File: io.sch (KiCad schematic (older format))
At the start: 14 parts, among them J5 USB_C_Receptacle_USB2.0, J6 Conn_ARM_JTAG_SWD_10, J7 UART, J8 Conn_02x14_Top_Bottom

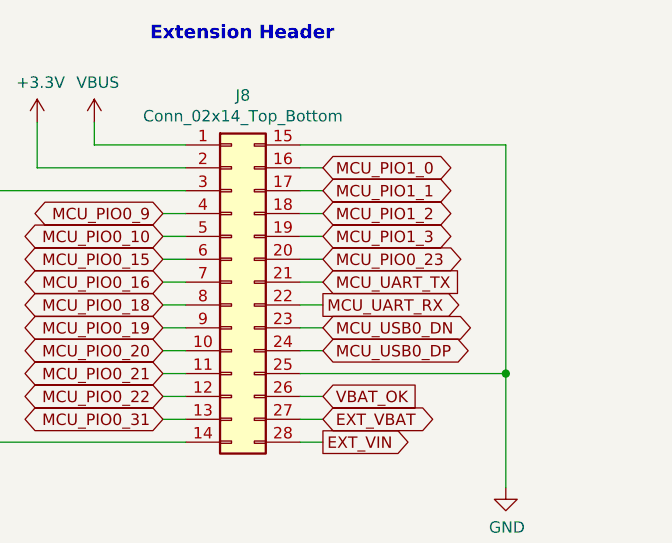
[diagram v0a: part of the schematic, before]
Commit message: Fixed issue #2, #3, #4 and #5
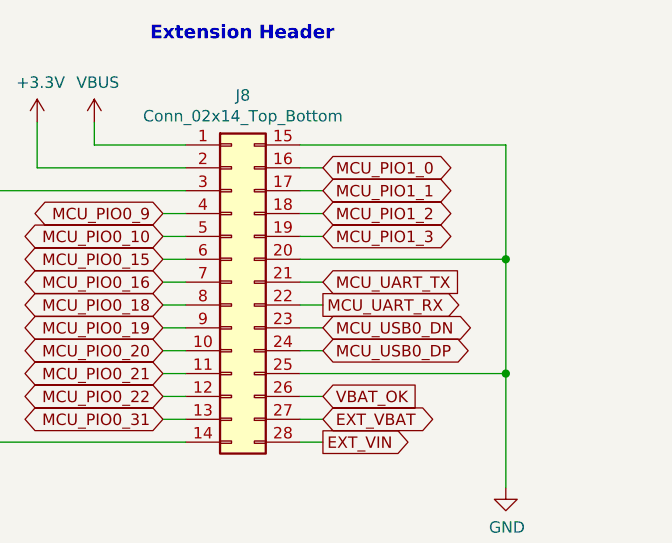
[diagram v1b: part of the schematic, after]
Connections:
- net MCU_PIO0_23 is gone; now on net GND: J8.20 (Pin_20)
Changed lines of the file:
@@
 Sheet 6 6
 Title "Tardigrade"
-Date "2020-09-24"
+Date "2020-11-05"
 Rev "1.0"
 Comp "Lucerne University of Applied Sciences and Arts"
@@
 	3700 1600 4000 1600
 Wire Wire Line
-	9200 1650 9200 2650
-Text GLabel 8400 2150 2    50   BiDi ~ 0
-MCU_PIO0_23
-Wire Wire Line
-	8400 2150 8300 2150
+	9200 1650 9200 2150
 Wire Wire Line
 	3350 1600 3400 1600
@@
 	1    0    0    -1
 $EndComp
+Wire Wire Line
+	8300 2150 9200 2150
+Connection ~ 9200 2150
+Wire Wire Line
+	9200 2150 9200 2650
 $EndSCHEMATC

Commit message: Removed jumpers from ios
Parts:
- removed JP15: Jumper_NC_Small, Jumper:SolderJumper-2_P1.3mm_Bridged_Pad1.0x1.5mm, symbol Device:Jumper_NC_Small
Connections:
- net +3V3: now also J6.1 (VTref)
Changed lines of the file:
@@
 Wire Wire Line
 	3450 5950 3450 5900
-$Comp
-L Device:Jumper_NC_Small JP?
-U 1 1 5FB371B1
-P 3450 4550
-AR Path="/5F6D82DD/5FB371B1" Ref="JP?"  Part="1"
-AR Path="/5F6D9EB2/5FB371B1" Ref="JP15"  Part="1"
-F 0 "JP15" V 3450 4502 50  0000 R CNN
-F 1 "Jumper_NC_Small" V 3405 4503 50  0001 R CNN
-F 2 "Jumper:SolderJumper-2_P1.3mm_Bridged_Pad1.0x1.5mm" H 3450 4550 50  0001 C CNN
-F 3 "~" H 3450 4550 50  0001 C CNN
-	1    3450 4550
-	0    -1   -1   0
-$EndComp
-Wire Wire Line
-	3450 4700 3450 4650
-Wire Wire Line
-	3450 4450 3450 4400
 Text Notes 2200 6600 0    50   Italic 0
 The JTAG functions TRST, TCK, TMS, TDI, and TDO, are selected \non pins PIO0_2 to PIO0_6 by hardware when the part is in \nboundary scan mode. The JTAG functions cannot be used for \ndebug mode
@@
 Extension Header
 $Comp
-L power:PWR_FLAG #FLG07
-U 1 1 5FCBE7BD
-P 3300 4650
-F 0 "#FLG07" H 3300 4725 50  0001 C CNN
-F 1 "PWR_FLAG" H 3300 4823 50  0001 C CNN
-F 2 "" H 3300 4650 50  0001 C CNN
-F 3 "~" H 3300 4650 50  0001 C CNN
-	1    3300 4650
-	1    0    0    -1
-$EndComp
-Wire Wire Line
-	3450 4700 3300 4700
-Wire Wire Line
-	3300 4700 3300 4650
-Connection ~ 3450 4700
-$Comp
 L Mechanical:MountingHole H?
 U 1 1 5FDA315D
@@
 L power:+3.3V #PWR067
 U 1 1 5F833987
-P 3450 4400
-F 0 "#PWR067" H 3450 4250 50  0001 C CNN
-F 1 "+3.3V" H 3465 4573 50  0000 C CNN
-F 2 "" H 3450 4400 50  0001 C CNN
-F 3 "" H 3450 4400 50  0001 C CNN
-	1    3450 4400
+P 3450 4650
+F 0 "#PWR067" H 3450 4500 50  0001 C CNN
+F 1 "+3.3V" H 3465 4823 50  0000 C CNN
+F 2 "" H 3450 4650 50  0001 C CNN
+F 3 "" H 3450 4650 50  0001 C CNN
+	1    3450 4650
 	1    0    0    -1
 $EndComp
@@
 Wire Wire Line
 	9200 2150 9200 2650
+Wire Wire Line
+	3450 4650 3450 4700
 $EndSCHEMATC

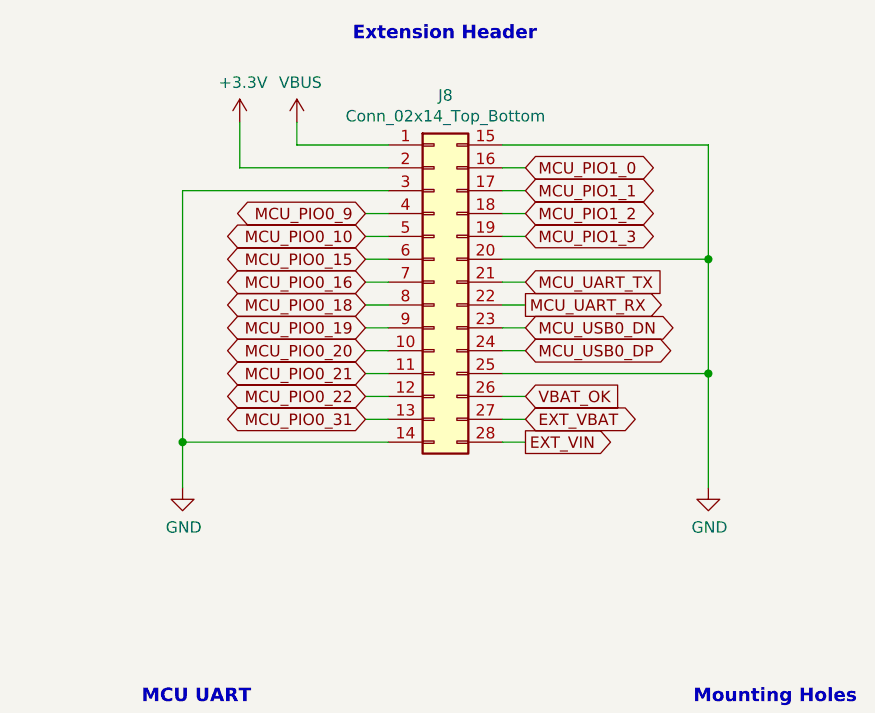
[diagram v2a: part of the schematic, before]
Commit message: Changed extension header symbol
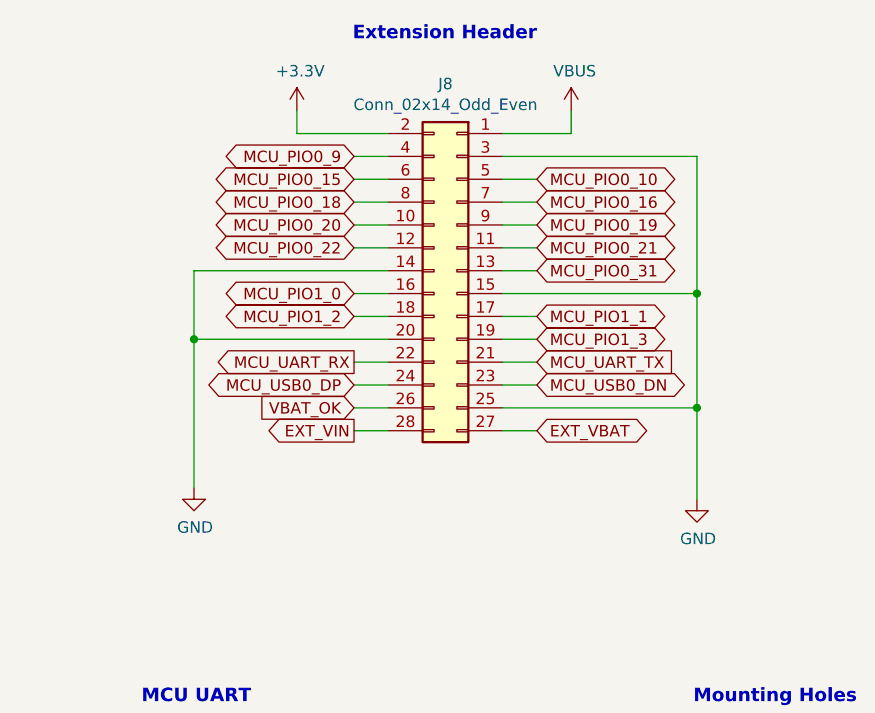
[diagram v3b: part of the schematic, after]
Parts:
- removed J8: Conn_02x14_Top_Bottom, Connector_PinSocket_2.54mm:PinSocket_2x14_P2.54mm_Vertical, symbol Connector_Generic:Conn_02x14_Top_Bottom
- added J8: Conn_02x14_Odd_Even, symbol Connector_Generic:Conn_02x14_Odd_Even
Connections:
- net +3V3: now also J8.2 (Pin_2)
- net EXT_VBAT: now also J8.27 (Pin_27)
- net EXT_VIN: now also J8.28 (Pin_28)
- net GND: now also J8.14 (Pin_14), J8.15 (Pin_15), J8.20 (Pin_20), J8.25 (Pin_25), J8.3 (Pin_3)
- net MCU_PIO0_10: now also J8.5 (Pin_5)
- net MCU_PIO0_15: now also J8.6 (Pin_6)
- net MCU_PIO0_16: now also J8.7 (Pin_7)
- net MCU_PIO0_18: now also J8.8 (Pin_8)
- net MCU_PIO0_19: now also J8.9 (Pin_9)
- net MCU_PIO0_20: now also J8.10 (Pin_10)
- net MCU_PIO0_21: now also J8.11 (Pin_11)
- net MCU_PIO0_22: now also J8.12 (Pin_12)
- net MCU_PIO0_31: now also J8.13 (Pin_13)
- net MCU_PIO0_9: now also J8.4 (Pin_4)
- net MCU_PIO1_0: now also J8.16 (Pin_16)
- net MCU_PIO1_1: now also J8.17 (Pin_17)
- net MCU_PIO1_2: now also J8.18 (Pin_18)
- net MCU_PIO1_3: now also J8.19 (Pin_19)
- net MCU_UART_RX: now also J8.22 (Pin_22)
- net MCU_UART_TX: now also J8.21 (Pin_21)
- net MCU_USB0_DN: now also J8.23 (Pin_23)
- net MCU_USB0_DP: now also J8.24 (Pin_24)
- net VBAT_OK: now also J8.26 (Pin_26)
- net VBUS: now also J8.1 (Pin_1)
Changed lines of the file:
@@
 Text Notes 3050 1200 2    59   ~ 12
 High-Speed USB 2.0 (USB-C)
-Text GLabel 8400 2750 2    50   Input ~ 0
-VBAT_OK
-Text GLabel 8400 1750 2    50   BiDi ~ 0
-MCU_PIO1_0
-Text GLabel 7700 2250 0    50   BiDi ~ 0
-MCU_PIO0_16
-Text GLabel 7700 2150 0    50   BiDi ~ 0
-MCU_PIO0_15
-Text GLabel 7700 2850 0    50   BiDi ~ 0
-MCU_PIO0_31
-Text GLabel 7700 2050 0    50   BiDi ~ 0
-MCU_PIO0_10
-Text GLabel 7700 2550 0    50   BiDi ~ 0
-MCU_PIO0_20
-Text GLabel 8400 2050 2    50   BiDi ~ 0
-MCU_PIO1_3
-Text GLabel 8400 1950 2    50   BiDi ~ 0
-MCU_PIO1_2
-Text GLabel 8400 1850 2    50   BiDi ~ 0
-MCU_PIO1_1
-Text GLabel 7700 2350 0    50   BiDi ~ 0
-MCU_PIO0_18
-Text GLabel 7700 1950 0    50   BiDi ~ 0
-MCU_PIO0_9
-Text GLabel 8400 2450 2    50   BiDi ~ 0
-MCU_USB0_DN
-Text GLabel 7700 2450 0    50   BiDi ~ 0
-MCU_PIO0_19
-Text GLabel 7700 2750 0    50   BiDi ~ 0
-MCU_PIO0_22
-Text GLabel 7700 2650 0    50   BiDi ~ 0
-MCU_PIO0_21
-Text GLabel 8400 2350 2    50   Output ~ 0
-MCU_UART_RX
-Text GLabel 8400 2250 2    50   Input ~ 0
-MCU_UART_TX
-Text GLabel 8400 2550 2    50   BiDi ~ 0
-MCU_USB0_DP
 $Comp
 L Connector_Generic:Conn_01x03 J7
@@
 Wire Wire Line
 	6350 4700 6450 4700
-Text GLabel 8400 2850 2    50   BiDi ~ 0
-EXT_VBAT
-Text GLabel 8400 2950 2    50   Output ~ 0
-EXT_VIN
-$Comp
-L Connector_Generic:Conn_02x14_Top_Bottom J8
-U 1 1 5F9A21A1
-P 8000 2250
-F 0 "J8" H 8050 3067 50  0000 C CNN
-F 1 "Conn_02x14_Top_Bottom" H 8050 2976 50  0000 C CNN
-F 2 "Connector_PinSocket_2.54mm:PinSocket_2x14_P2.54mm_Vertical" H 8000 2250 50  0001 C CNN
-F 3 "~" H 8000 2250 50  0001 C CNN
-	1    8000 2250
-	1    0    0    -1
-$EndComp
-$Comp
-L power:+3.3V #PWR074
-U 1 1 5F9A457A
-P 7150 1550
-F 0 "#PWR074" H 7150 1400 50  0001 C CNN
-F 1 "+3.3V" H 7165 1723 50  0000 C CNN
-F 2 "" H 7150 1550 50  0001 C CNN
-F 3 "" H 7150 1550 50  0001 C CNN
-	1    7150 1550
-	1    0    0    -1
-$EndComp
-$Comp
-L power:GND #PWR076
-U 1 1 5FA0CA24
-P 9200 3150
-F 0 "#PWR076" H 9200 2900 50  0001 C CNN
-F 1 "GND" H 9205 2977 50  0000 C CNN
-F 2 "" H 9200 3150 50  0001 C CNN
-F 3 "" H 9200 3150 50  0001 C CNN
-	1    9200 3150
-	1    0    0    -1
-$EndComp
-$Comp
-L power:GND #PWR072
-U 1 1 5FA0D50C
-P 6900 3150
-F 0 "#PWR072" H 6900 2900 50  0001 C CNN
-F 1 "GND" H 6905 2977 50  0000 C CNN
-F 2 "" H 6900 3150 50  0001 C CNN
-F 3 "" H 6900 3150 50  0001 C CNN
-	1    6900 3150
-	1    0    0    -1
-$EndComp
-Wire Wire Line
-	8300 1650 9200 1650
-Wire Wire Line
-	8300 2650 9200 2650
-Connection ~ 9200 2650
-Wire Wire Line
-	9200 2650 9200 3150
-Wire Wire Line
-	7800 1850 6900 1850
-Wire Wire Line
-	6900 1850 6900 2950
-Wire Wire Line
-	7800 2950 6900 2950
-Connection ~ 6900 2950
-Wire Wire Line
-	6900 2950 6900 3150
-Wire Wire Line
-	8400 1750 8300 1750
-Wire Wire Line
-	8400 1850 8300 1850
-Wire Wire Line
-	8400 1950 8300 1950
-Wire Wire Line
-	8400 2050 8300 2050
-Wire Wire Line
-	8400 2250 8300 2250
-Wire Wire Line
-	8400 2350 8300 2350
-Wire Wire Line
-	8400 2450 8300 2450
-Wire Wire Line
-	8400 2550 8300 2550
-Wire Wire Line
-	8400 2750 8300 2750
-Wire Wire Line
-	8400 2850 8300 2850
-Wire Wire Line
-	8400 2950 8300 2950
-Wire Wire Line
-	7700 2850 7800 2850
-Wire Wire Line
-	7800 2750 7700 2750
-Wire Wire Line
-	7700 2650 7800 2650
-Wire Wire Line
-	7800 2550 7700 2550
-Wire Wire Line
-	7700 2450 7800 2450
-Wire Wire Line
-	7800 2350 7700 2350
-Wire Wire Line
-	7700 2250 7800 2250
-Wire Wire Line
-	7800 2150 7700 2150
-Wire Wire Line
-	7700 2050 7800 2050
-Wire Wire Line
-	7800 1950 7700 1950
 Text Notes 8450 1200 2    59   ~ 12
 Extension Header
@@
 Wire Wire Line
 	3250 2300 3300 2300
-Wire Wire Line
-	7150 1750 7150 1550
-Wire Wire Line
-	7800 1750 7150 1750
-$Comp
-L power:VBUS #PWR075
-U 1 1 5F830396
-P 7400 1550
-F 0 "#PWR075" H 7400 1400 50  0001 C CNN
-F 1 "VBUS" H 7415 1723 50  0000 C CNN
-F 2 "" H 7400 1550 50  0001 C CNN
-F 3 "" H 7400 1550 50  0001 C CNN
-	1    7400 1550
-	1    0    0    -1
-$EndComp
-Wire Wire Line
-	7400 1550 7400 1650
-Wire Wire Line
-	7400 1650 7800 1650
 $Comp
 L power:+3.3V #PWR067
@@
 	3700 1600 4000 1600
 Wire Wire Line
-	9200 1650 9200 2150
-Wire Wire Line
 	3350 1600 3400 1600
 Wire Wire Line
@@
 $EndComp
 Wire Wire Line
-	8300 2150 9200 2150
-Connection ~ 9200 2150
-Wire Wire Line
-	9200 2150 9200 2650
-Wire Wire Line
 	3450 4650 3450 4700
+$Comp
+L Connector_Generic:Conn_02x14_Odd_Even J8
+U 1 1 5FAF0C03
+P 8100 2200
+F 0 "J8" H 8150 3017 50  0000 C CNN
+F 1 "Conn_02x14_Odd_Even" H 8150 2926 50  0000 C CNN
+F 2 "" H 8100 2200 50  0001 C CNN
+F 3 "~" H 8100 2200 50  0001 C CNN
+	1    8100 2200
+	-1   0    0    -1
+$EndComp
+Text GLabel 7650 1700 0    50   BiDi ~ 0
+MCU_PIO0_9
+Text GLabel 8450 1800 2    50   BiDi ~ 0
+MCU_PIO0_10
+Text GLabel 7650 1800 0    50   BiDi ~ 0
+MCU_PIO0_15
+Text GLabel 7650 1900 0    50   BiDi ~ 0
+MCU_PIO0_18
+Text GLabel 7650 2000 0    50   BiDi ~ 0
+MCU_PIO0_20
+Text GLabel 7650 2100 0    50   BiDi ~ 0
+MCU_PIO0_22
+Text GLabel 7650 2300 0    50   BiDi ~ 0
+MCU_PIO1_0
+Text GLabel 7650 2400 0    50   BiDi ~ 0
+MCU_PIO1_2
+Text GLabel 7650 2600 0    50   Output ~ 0
+MCU_UART_RX
+Text GLabel 7650 2700 0    50   BiDi ~ 0
+MCU_USB0_DP
+Text GLabel 7650 2800 0    50   Input ~ 0
+VBAT_OK
+Text GLabel 7650 2900 0    50   Output ~ 0
+EXT_VIN
+Text GLabel 8450 1900 2    50   BiDi ~ 0
+MCU_PIO0_16
+Text GLabel 8450 2000 2    50   BiDi ~ 0
+MCU_PIO0_19
+Text GLabel 8450 2100 2    50   BiDi ~ 0
+MCU_PIO0_21
+Text GLabel 8450 2200 2    50   BiDi ~ 0
+MCU_PIO0_31
+Text GLabel 8450 2400 2    50   BiDi ~ 0
+MCU_PIO1_1
+Text GLabel 8450 2500 2    50   BiDi ~ 0
+MCU_PIO1_3
+Text GLabel 8450 2600 2    50   Input ~ 0
+MCU_UART_TX
+Text GLabel 8450 2700 2    50   BiDi ~ 0
+MCU_USB0_DN
+Text GLabel 8450 2900 2    50   BiDi ~ 0
+EXT_VBAT
+$Comp
+L power:GND #PWR?
+U 1 1 5FB15973
+P 6950 3150
+F 0 "#PWR?" H 6950 2900 50  0001 C CNN
+F 1 "GND" H 6955 2977 50  0000 C CNN
+F 2 "" H 6950 3150 50  0001 C CNN
+F 3 "" H 6950 3150 50  0001 C CNN
+	1    6950 3150
+	1    0    0    -1
+$EndComp
+$Comp
+L power:GND #PWR?
+U 1 1 5FB15D4A
+P 9150 3200
+F 0 "#PWR?" H 9150 2950 50  0001 C CNN
+F 1 "GND" H 9155 3027 50  0000 C CNN
+F 2 "" H 9150 3200 50  0001 C CNN
+F 3 "" H 9150 3200 50  0001 C CNN
+	1    9150 3200
+	1    0    0    -1
+$EndComp
+Wire Wire Line
+	8300 1700 9150 1700
+Wire Wire Line
+	9150 1700 9150 2300
+Wire Wire Line
+	7800 2200 6950 2200
+Wire Wire Line
+	6950 2200 6950 2500
+Wire Wire Line
+	7800 2500 6950 2500
+Connection ~ 6950 2500
+Wire Wire Line
+	6950 2500 6950 3150
+Wire Wire Line
+	8300 2300 9150 2300
+Connection ~ 9150 2300
+Wire Wire Line
+	9150 2300 9150 2800
+Wire Wire Line
+	8300 2800 9150 2800
+Connection ~ 9150 2800
+Wire Wire Line
+	9150 2800 9150 3200
+$Comp
+L power:VBUS #PWR?
+U 1 1 5FB21530
+P 8600 1500
+F 0 "#PWR?" H 8600 1350 50  0001 C CNN
+F 1 "VBUS" H 8615 1673 50  0000 C CNN
+F 2 "" H 8600 1500 50  0001 C CNN
+F 3 "" H 8600 1500 50  0001 C CNN
+	1    8600 1500
+	1    0    0    -1
+$EndComp
+Wire Wire Line
+	8300 1600 8600 1600
+Wire Wire Line
+	8600 1600 8600 1500
+$Comp
+L power:+3.3V #PWR?
+U 1 1 5FB24107
+P 7400 1500
+F 0 "#PWR?" H 7400 1350 50  0001 C CNN
+F 1 "+3.3V" H 7415 1673 50  0000 C CNN
+F 2 "" H 7400 1500 50  0001 C CNN
+F 3 "" H 7400 1500 50  0001 C CNN
+	1    7400 1500
+	1    0    0    -1
+$EndComp
+Wire Wire Line
+	7400 1500 7400 1600
+Wire Wire Line
+	7400 1600 7800 1600
+Wire Wire Line
+	7650 1700 7800 1700
+Wire Wire Line
+	7800 1800 7650 1800
+Wire Wire Line
+	7650 1900 7800 1900
+Wire Wire Line
+	7800 2000 7650 2000
+Wire Wire Line
+	7650 2100 7800 2100
+Wire Wire Line
+	7800 2300 7650 2300
+Wire Wire Line
+	7650 2400 7800 2400
+Wire Wire Line
+	7800 2600 7650 2600
+Wire Wire Line
+	7650 2700 7800 2700
+Wire Wire Line
+	7800 2800 7650 2800
+Wire Wire Line
+	7650 2900 7800 2900
+Wire Wire Line
+	8300 2900 8450 2900
+Wire Wire Line
+	8300 2700 8450 2700
+Wire Wire Line
+	8300 2600 8450 2600
+Wire Wire Line
+	8450 2500 8300 2500
+Wire Wire Line
+	8300 2400 8450 2400
+Wire Wire Line
+	8450 2200 8300 2200
+Wire Wire Line
+	8300 2100 8450 2100
+Wire Wire Line
+	8450 2000 8300 2000
+Wire Wire Line
+	8300 1900 8450 1900
+Wire Wire Line
+	8450 1800 8300 1800
 $EndSCHEMATC
